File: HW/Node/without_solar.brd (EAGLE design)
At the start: 45.1 x 30.1 mm, 16 parts, among them U1 MS560702BA03-50, U2 HDC2080DMBR, U3 RFM69HW, X1 734120110

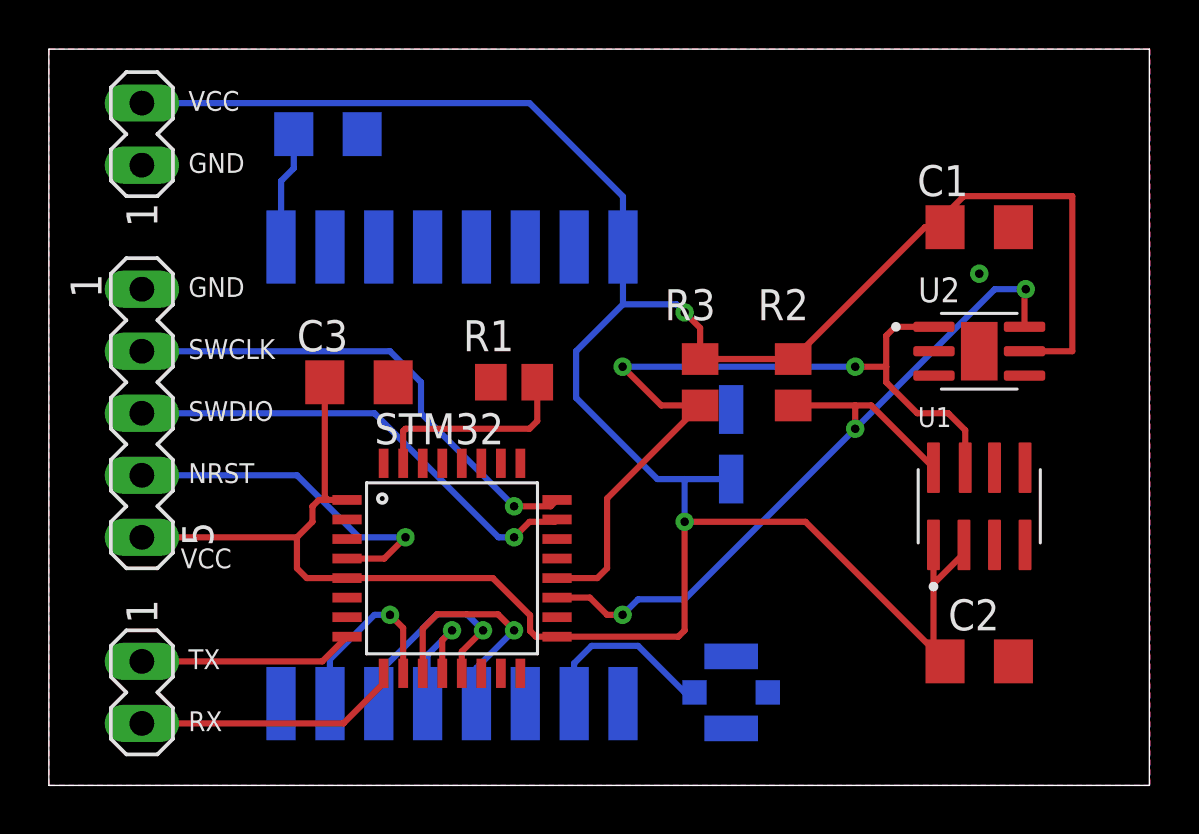
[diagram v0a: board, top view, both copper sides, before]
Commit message: HW: Update node schematic and board
Signed-off-by: Ales Musil <aedvin1@gmail.com>
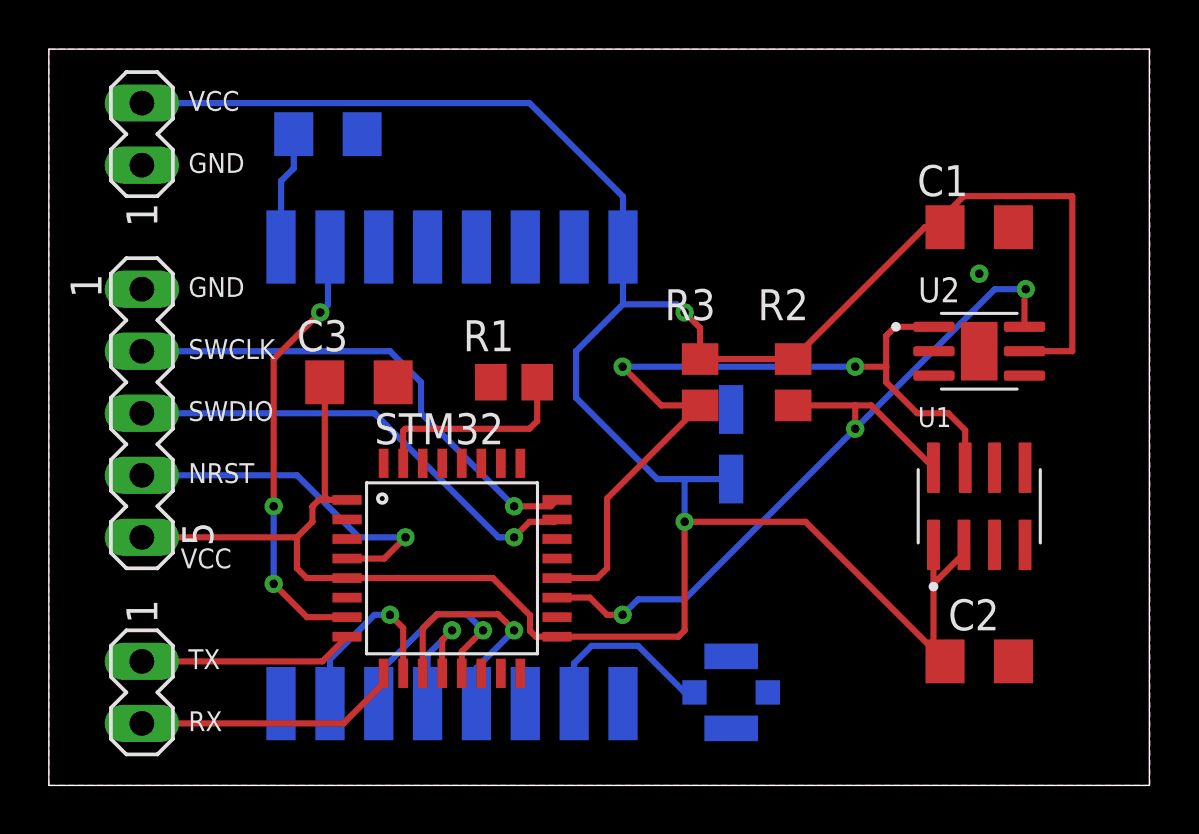
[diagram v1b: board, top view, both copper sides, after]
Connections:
- new net RFM_INT: STM32.7, U3.2
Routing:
- net RFM_INT: track 0.00 -> 18.3 mm, vias 0 -> 3
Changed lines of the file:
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@@
 <vertex x="45.085" y="0"/>
 <vertex x="0" y="0"/>
-<vertex x="0" y="30.1625"/>
 </polygon>
 </signal>
@@
 <wire x1="10.03" y1="25.27" x2="9.51" y2="24.75" width="0.254" layer="16"/>
 </signal>
+<signal name="RFM_INT">
+<contactref element="STM32" pad="7"/>
+<contactref element="U3" pad="2"/>
+<via x="11.1125" y="19.3675" extent="1-16" drill="0.35"/>
+<via x="9.2075" y="11.43" extent="1-16" drill="0.35"/>
+<via x="9.2075" y="8.255" extent="1-16" drill="0.35"/>
+<wire x1="12.21" y1="6.89" x2="10.5725" y2="6.89" width="0.254" layer="1"/>
+<wire x1="10.5725" y1="6.89" x2="9.2075" y2="8.255" width="0.254" layer="1"/>
+<wire x1="11.1125" y1="19.3675" x2="9.2075" y2="17.4625" width="0.254" layer="1"/>
+<wire x1="9.2075" y1="17.4625" x2="9.2075" y2="11.43" width="0.254" layer="1"/>
+<wire x1="11.1125" y1="19.3675" x2="11.43" y2="19.685" width="0.254" layer="16"/>
+<wire x1="11.43" y1="21.97" x2="11.51" y2="22.05" width="0.254" layer="16"/>
+<wire x1="11.43" y1="19.685" x2="11.43" y2="21.97" width="0.254" layer="16"/>
+<wire x1="9.2075" y1="8.255" x2="9.2075" y2="11.43" width="0.254" layer="16"/>
+</signal>
 </signals>
